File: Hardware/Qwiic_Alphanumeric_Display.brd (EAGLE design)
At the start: 40.6 x 30.5 mm, 32 parts, among them J1 PTH, J2 Qwiic Right Angle, U2 HT16K33

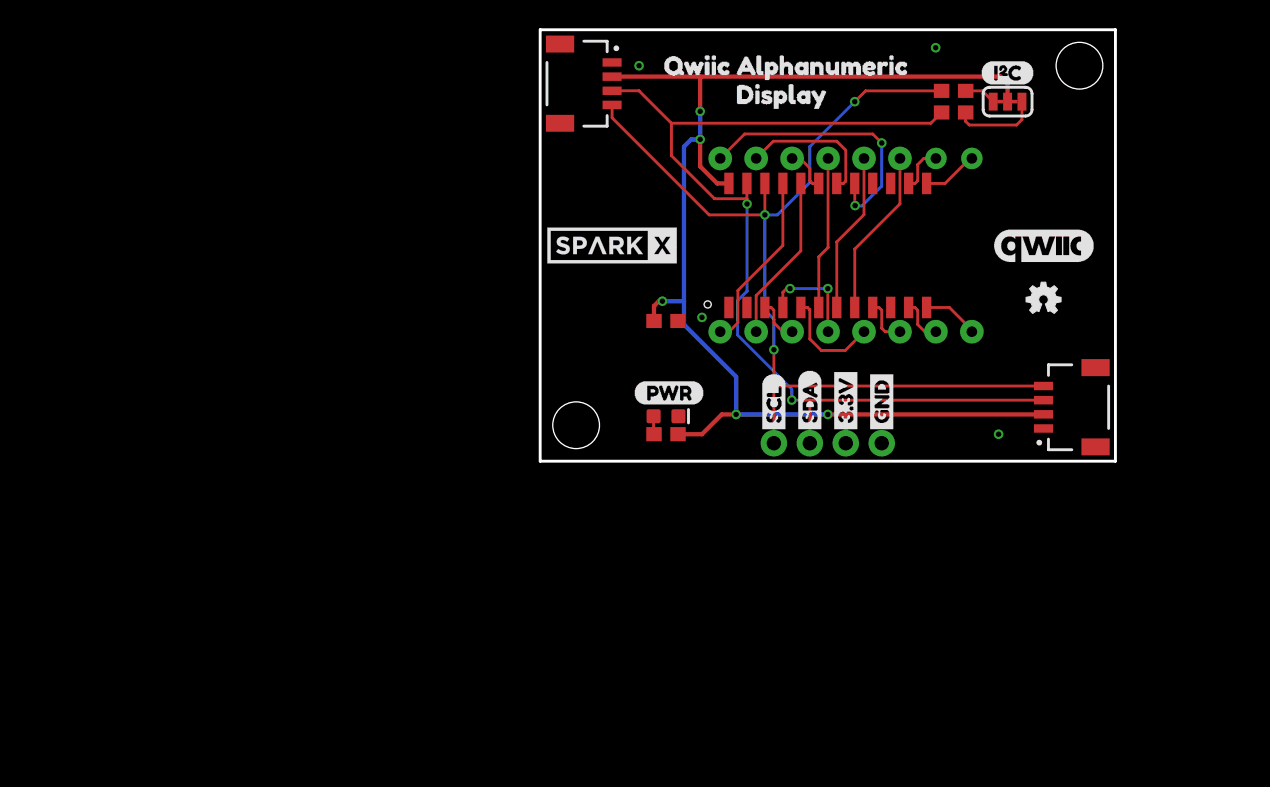
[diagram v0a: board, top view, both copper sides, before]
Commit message: New pin assignments
Next: route address jumpers, etc
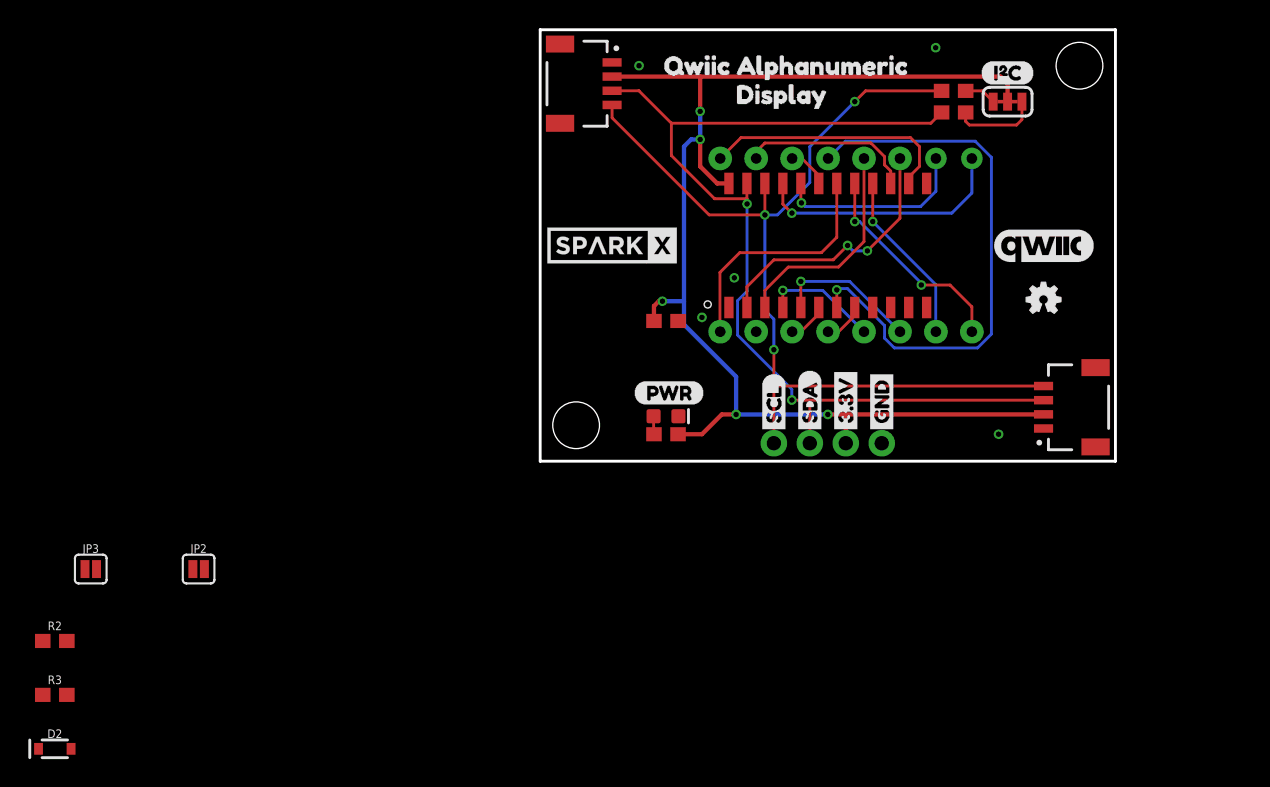
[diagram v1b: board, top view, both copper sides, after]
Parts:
- added D2: 250mA/100V, SparkFun-DiscreteSemi:SOD-323
- added JP2, JP3: JUMPER-SMT_2_NO_SILK, SparkFun-Jumpers:SMT-JUMPER_2_NO_SILK
- added R2, R3: 39k, SparkFun-Resistors:0603
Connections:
- removed net COM_G1: U1.5, U2.4
- new net COM_G: U1.5, U2.8
- new net N$2: JP2.2, R2.1
- new net N$3: JP3.2, R3.1
- new net N$6: D2.C, R2.2, R3.2
- net COM_A: now also D2.A, U2.2; no longer U2.8
- net COM_B: now also U2.3; no longer U2.7
- net COM_C: now also U2.4; no longer U2.5
- net COM_D: now also U2.5; no longer U2.9
- net COM_E: now also U2.6; no longer U2.3
- net COM_F: now also U2.7; no longer U2.6
- net DIG_1A: now also JP2.1, U2.21; no longer U2.13
- net DIG_1B: now also U2.17; no longer U2.12
- net DIG_2A: now also JP3.1, U2.20; no longer U2.14
- net DIG_2B: now also U2.16; no longer U2.11
- net DIG_3B: now also U2.15; no longer U2.18
- net DIG_4A: now also U2.18; no longer U2.21
- net DIG_4B: now also U2.14; no longer U2.17
- net DIG_DP: now also U2.13; no longer U2.20
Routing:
- net COM_F: track 10.8 -> 39.9 mm, vias 0 -> 1
- net DIG_1A: track 3.92 -> 18.1 mm, vias 0 -> 1
- net DIG_DP: track 11.8 -> 0.00 mm
- net DIG_1B: track 3.97 -> 15.3 mm, vias 0 -> 2
- net DIG_2A: track 3.32 -> 13.8 mm, vias 0 -> 1
- net DIG_2B: track 3.23 -> 12.3 mm, vias 0 -> 1
- net COM_G1: track 7.41 -> 0.00 mm, vias 2 -> 0
- net COM_A: track 11.9 -> 18.8 mm, vias 0 -> 2
- net COM_D: track 3.38 -> 10.3 mm, vias 0 -> 1
- net DIG_4A: track 12.7 -> 17.3 mm
- net COM_B: track 11.3 -> 15.5 mm
- net COM_G: track 0.00 -> 2.93 mm
- net DIG_3B: track 9.99 -> 12.3 mm
- net DIG_4B: track 19.5 -> 17.9 mm, vias 2 -> 0
- net COM_C: track 7.47 -> 8.15 mm, vias 0 -> 1

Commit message: Rev X02 of Qwiic Alpha?
Still needs Nate's look-over. Tighter layout, mounting holes, address/power jumpers. Needs V score lines? Where will the silkscreen go?
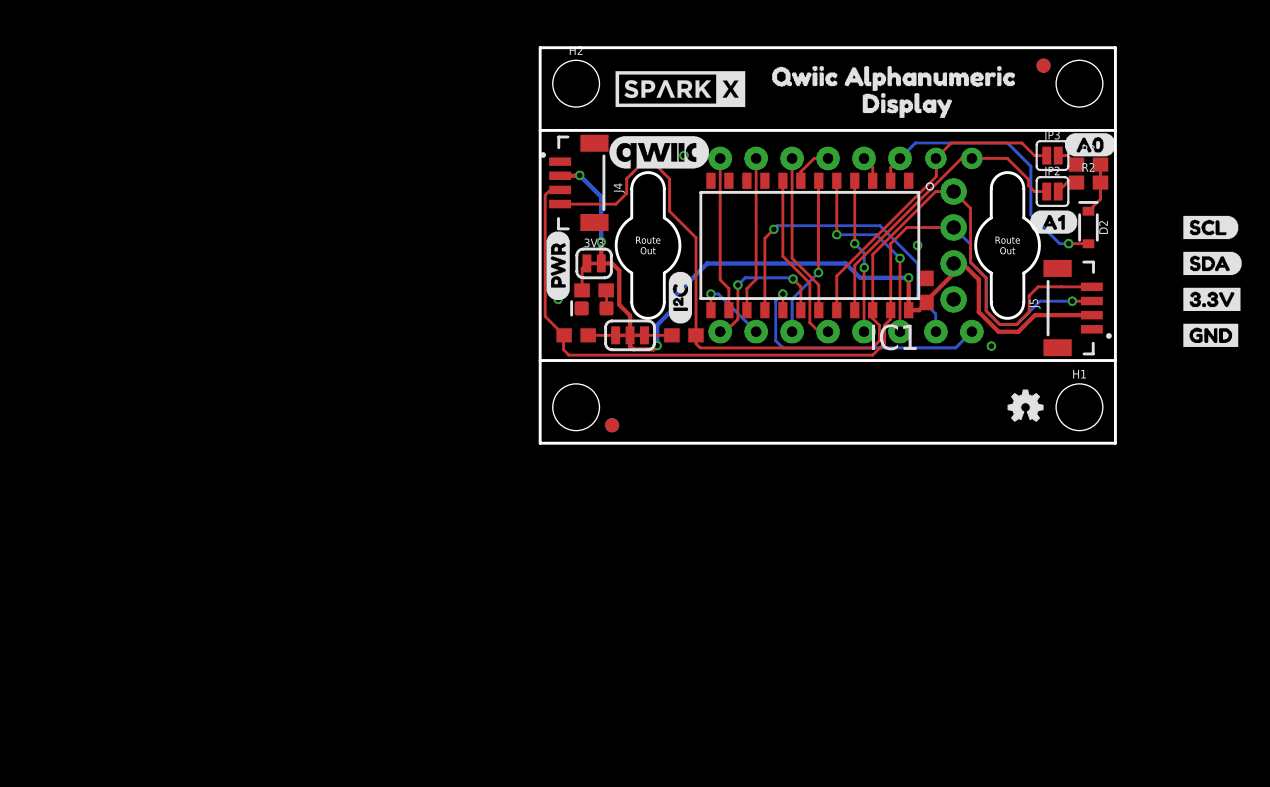
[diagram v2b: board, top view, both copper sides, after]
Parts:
- removed J1: PTH, SparkFun-Connectors:JST04_1MM_RA
- removed J2: Qwiic Right Angle, SparkFun-Connectors:JST04_1MM_RA
- removed U$6: (no value), buzzard_labels:3#3V1
- removed U$7: (no value), buzzard_labels:GND0
- removed U$8: (no value), buzzard_labels:SCL3
- removed U$9: (no value), buzzard_labels:SDA2
- removed U2: HT16K33, Alphanumeric_Display_Library:HT16K33
- added 3V3: JUMPER-SMT_2_NC_TRACE_SILK, SparkFun-Jumpers:SMT-JUMPER_2_NC_TRACE_SILK
- added FD1, FD2, FD3, FD4: FIDUCIAL1X2, SparkFun-Aesthetics:FIDUCIAL-1X2
- added H1, H2: STAND-OFF, SparkFun-Hardware:STAND-OFF
- added IC1: (no value), Alphanumeric_Display_Library:HT16K33
- added J4, J5: Vertical Qwiic Connector, SparkFun-Connectors:JST04_1MM_VERT
- added U$18, U$19: MOUNTING_HOLE_M2-0.4X6, Alphanumeric_Display_Library:MOUNTING_HOLE_M2-0.4X6
- added U$20: (no value), buzzard_labels (63):A00
- added U$21: (no value), buzzard_labels (63):A11
- moved R3 82.1 mm to (38.7, 21.0)
- moved D2 81.8 mm to (38.7, 16.5), turned to 270 degrees
- moved R2 79.9 mm to (38.7, 19.7)
- moved JP3 74.0 mm to (36.2, 21.6)
- moved JP2 66.0 mm to (36.2, 19.1)
- moved U$4 32.0 mm to (45.0, 16.5), turned to 0 degrees
- moved I2C 31.4 mm to (6.35, 8.89), turned to 180 degrees
- moved R4 31.0 mm to (2.54, 8.89)
- moved U$5 28.6 mm to (45.0, 14.0), turned to 0 degrees
- moved U$11 28.0 mm to (8.38, 21.8)
- moved U$10 27.7 mm to (9.91, 9.65), turned to 90 degrees
- moved R5 25.7 mm to (10.2, 8.89), turned to 180 degrees
- moved U$1 25.3 mm to (45.0, 11.4), turned to 0 degrees
- moved U$14 23.6 mm to (30.5, 26.3)
- moved U$2 22.0 mm to (45.0, 8.89), turned to 0 degrees
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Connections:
- new net N$7: 3V3.1, R1.2
- net 3.3V: now also 3V3.2, IC1.24, J4.2, J5.2; no longer J1.2, J2.2, R1.2, U2.24
- net COM_A: now also IC1.2; no longer U2.2
- net COM_B: now also IC1.3; no longer U2.3
- net COM_C: now also IC1.4; no longer U2.4
- net COM_D: now also IC1.5; no longer U2.5
- net COM_E: now also IC1.6; no longer U2.6
- net COM_F: now also IC1.7; no longer U2.7
- net COM_G: now also IC1.8; no longer U2.8
- net DIG_1A: now also IC1.21; no longer U2.21
- net DIG_1B: now also IC1.17; no longer U2.17
- net DIG_2A: now also IC1.20; no longer U2.20
- net DIG_2B: now also IC1.16; no longer U2.16
- net DIG_3A: now also IC1.19; no longer U2.19
- net DIG_3B: now also IC1.15; no longer U2.15
- net DIG_4A: now also IC1.18; no longer U2.18
- net DIG_4B: now also IC1.14; no longer U2.14
- net DIG_DP: now also IC1.13; no longer U2.13
- net GND: now also IC1.1, J4.1, J5.1; no longer J1.1, J2.1, U2.1
- net SCL: now also IC1.22, J4.4, J5.4; no longer J1.4, J2.4, U2.22
- net SDA: now also IC1.23, J4.3, J5.3; no longer J1.3, J2.3, U2.23
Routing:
- net COM_F: track 39.9 -> 2.95 mm, vias 1 -> 0
- net 3.3V: track 91.8 -> 60.3 mm, vias 5 -> 4
- net COM_B: track 15.5 -> 1.83 mm
- net DIG_2B: track 12.3 -> 22.7 mm
- net COM_G: track 2.93 -> 12.4 mm
- net COM_E: track 2.86 -> 11.4 mm, vias 0 -> 1
- net DIG_3A: track 2.95 -> 11.5 mm
- net DIG_2A: track 13.8 -> 22.3 mm, vias 1 -> 0
- net SDA: track 71.5 -> 63.4 mm, vias 2 -> 1
- net DIG_4B: track 17.9 -> 11.0 mm
- net DIG_4A: track 17.3 -> 10.6 mm, vias 0 -> 2
- net DIG_DP: track 0.00 -> 5.44 mm, vias 0 -> 1
- net N$5: track 6.14 -> 1.94 mm
- net DIG_1B: track 15.3 -> 19.2 mm, vias 2 -> 1
- net COM_D: track 10.3 -> 14.1 mm, vias 1 -> 2
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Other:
- board size 40.6 x 30.5 mm -> 40.6 x 27.9 mm

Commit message: Rev X02 ordered!
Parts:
- removed JP1, JP8: STAND-OFF, SparkFun:STAND-OFF
- removed U$11: (no value), Labels:QWIIC_COPYRIGHT_MEDIUM
- removed U$12, U$14: (no value), SparkX:SPARKX-MEDIUM
- added H3, H4: STAND-OFF, SparkFun-Hardware:STAND-OFF
- added U$6: (no value), SparkFun-Aesthetics:QWIIC_4MM
- added U$7, U$8: SPARKX-LOGO4, SparkX:SPARKX-MEDIUM
- U$1: device buzzard_labels:3#3V1 -> buzzard_labels (65):32
- U$2: device buzzard_labels:GND0 -> buzzard_labels (65):C0
- U$4: device buzzard_labels:SCL3 -> buzzard_labels (65):D1
- U$5: device buzzard_labels:SDA2 -> buzzard_labels (65):G3
- moved U$2 18.4 mm to (29.6, 19.1)
- moved U$5 15.7 mm to (29.5, 11.4)
- moved U$1 15.4 mm to (29.6, 13.0)
- moved U$4 15.4 mm to (29.6, 17.7)
- moved JP2 0.63 mm to (35.6, 19.1)
- moved JP3 0.63 mm to (35.6, 21.6)
- moved R2 0.63 mm to (38.7, 19.1)
- moved R3 0.63 mm to (38.7, 20.3)
- moved U$20 0.46 mm to (36.7, 22.0)
- moved C1 0.13 mm to (27.4, 12.1)
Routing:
- net N$3: track 1.55 -> 2.44 mm
- net DIG_2A: track 22.3 -> 21.7 mm
- net DIG_1A: track 21.1 -> 20.4 mm
- net N$6: track 3.65 -> 3.01 mm
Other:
- outline, holes or cut-outs redrawn

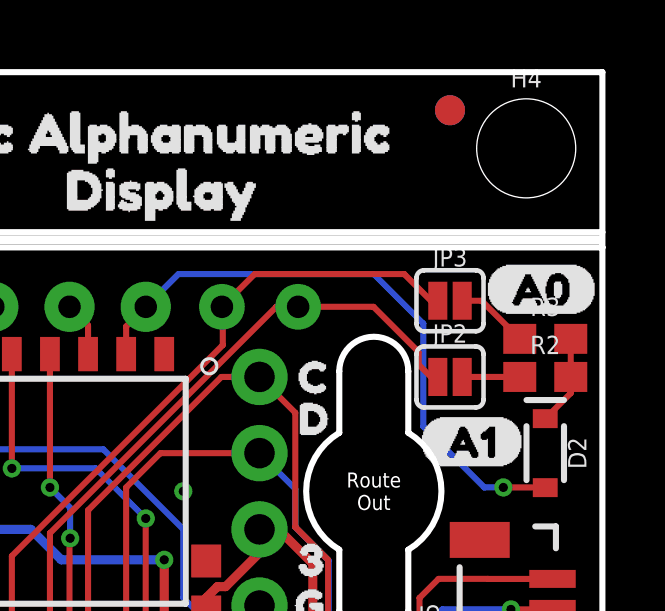
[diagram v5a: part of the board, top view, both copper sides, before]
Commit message: Rename jumpers to A0/A1/
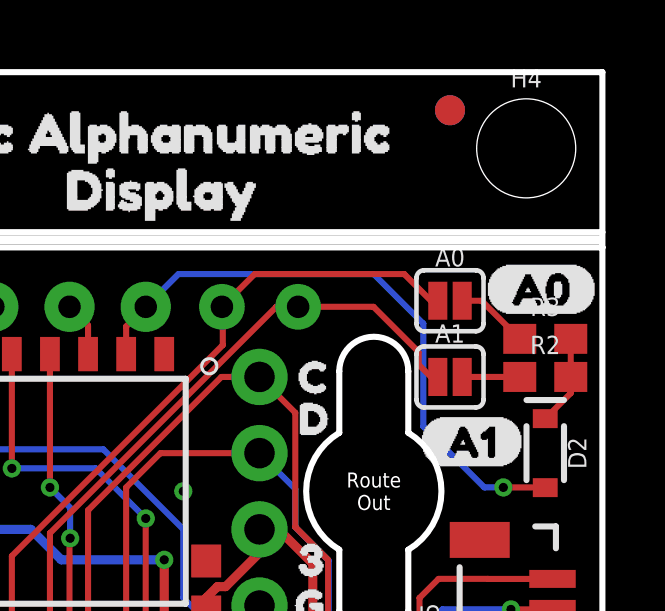
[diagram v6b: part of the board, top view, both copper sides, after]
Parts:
- renumbered JP2 to A1, JP3 to A0
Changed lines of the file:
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@@
 <?xml version="1.0" encoding="utf-8"?>
 <!DOCTYPE eagle SYSTEM "eagle.dtd">
-<eagle version="9.4.2">
+<eagle version="9.5.2">
 <drawing>
 <settings>
@@
 <element name="U$13" library="buzzard_labels (4)" package="QWIIC_ALPHANUMERIC0" value="" x="24.638" y="27.178" smashed="yes" rot="MR0"/>
 <element name="U$17" library="buzzard_labels (4)" package="DISPLAY1" value="" x="18.415" y="25.273" smashed="yes" rot="MR0"/>
-<element name="JP2" library="SparkFun-Jumpers" package="SMT-JUMPER_2_NO_SILK" package3d_urn="urn:adsk.eagle:package:39279/1" value="JUMPER-SMT_2_NO_SILK" x="35.56" y="19.05" smashed="yes">
+<element name="A1" library="SparkFun-Jumpers" package="SMT-JUMPER_2_NO_SILK" package3d_urn="urn:adsk.eagle:package:39279/1" value="JUMPER-SMT_2_NO_SILK" x="35.56" y="19.05" smashed="yes">
 <attribute name="NAME" x="35.56" y="20.193" size="0.6096" layer="25" font="vector" ratio="20" align="bottom-center"/>
 <attribute name="VALUE" x="35.56" y="17.907" size="0.6096" layer="27" font="vector" ratio="20" align="top-center"/>
 </element>
-<element name="JP3" library="SparkFun-Jumpers" package="SMT-JUMPER_2_NO_SILK" package3d_urn="urn:adsk.eagle:package:39279/1" value="JUMPER-SMT_2_NO_SILK" x="35.56" y="21.59" smashed="yes">
+<element name="A0" library="SparkFun-Jumpers" package="SMT-JUMPER_2_NO_SILK" package3d_urn="urn:adsk.eagle:package:39279/1" value="JUMPER-SMT_2_NO_SILK" x="35.56" y="21.59" smashed="yes">
 <attribute name="NAME" x="35.56" y="22.733" size="0.6096" layer="25" font="vector" ratio="20" align="bottom-center"/>
 <attribute name="VALUE" x="35.56" y="20.447" size="0.6096" layer="27" font="vector" ratio="20" align="top-center"/>
@@
 </signal>
 <signal name="DIG_1A">
-<contactref element="JP2" pad="1"/>
+<contactref element="A1" pad="1"/>
 <contactref element="U1" pad="16"/>
 <contactref element="IC1" pad="21"/>
@@
 </signal>
 <signal name="DIG_2A">
-<contactref element="JP3" pad="1"/>
+<contactref element="A0" pad="1"/>
 <contactref element="U1" pad="15"/>
 <contactref element="IC1" pad="20"/>
@@
 </signal>
 <signal name="N$2">
-<contactref element="JP2" pad="2"/>
+<contactref element="A1" pad="2"/>
 <contactref element="R2" pad="1"/>
 <wire x1="35.9664" y1="19.05" x2="37.885" y2="19.05" width="0.2032" layer="1"/>
 </signal>
 <signal name="N$3">
-<contactref element="JP3" pad="2"/>
+<contactref element="A0" pad="2"/>
 <contactref element="R3" pad="1"/>
 <wire x1="35.9664" y1="21.59" x2="36.615" y2="21.59" width="0.2032" layer="1"/>

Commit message: New decoupling cap
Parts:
- C1: value 0.1uF -> 1.0uF
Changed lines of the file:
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@@
 <?xml version="1.0" encoding="utf-8"?>
 <!DOCTYPE eagle SYSTEM "eagle.dtd">
-<eagle version="9.5.2">
+<eagle version="9.4.2">
 <drawing>
 <settings>
@@
 <layer number="44" name="Drills" color="7" fill="1" visible="no" active="yes"/>
 <layer number="45" name="Holes" color="7" fill="1" visible="yes" active="yes"/>
-<layer number="46" name="Milling" color="3" fill="1" visible="yes" active="yes"/>
+<layer number="46" name="Milling" color="3" fill="1" visible="no" active="yes"/>
 <layer number="47" name="Measures" color="7" fill="1" visible="no" active="yes"/>
 <layer number="48" name="Document" color="7" fill="1" visible="no" active="yes"/>
@@
 </autorouter>
 <elements>
-<element name="C1" library="SparkFun-Capacitors" package="0603" value="0.1uF" x="27.432" y="12.065" smashed="yes" rot="R90">
-<attribute name="PROD_ID" value="CAP-00810" x="92.202" y="52.705" size="1.778" layer="27" rot="R90" display="off"/>
+<element name="C1" library="SparkFun-Capacitors" package="0603" value="1.0uF" x="27.432" y="12.065" smashed="yes" rot="R90">
+<attribute name="PROD_ID" value="CAP-00868" x="92.202" y="52.705" size="1.778" layer="27" rot="R90" display="off"/>
 </element>
 <element name="D1" library="SparkFun-LED" package="LED-0603" value="RED" x="3.81" y="10.795" smashed="yes" rot="R180">
